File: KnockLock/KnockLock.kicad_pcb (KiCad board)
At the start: 2 copper layers, 90 x 60 mm, 60 parts, among them IC1 LM2575-3.3WT, IC2 ESP32-C3-WROOM-02-N4, J1 Boot Pins, J2 UART, J3 Battery Port, J4 Micro USB, J5 TBP04R12-500-03BE, M2 MountingHole_2.2mm_M2_ISO7380, Q1 BC547B, Q2 IRLML6402TRPBF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

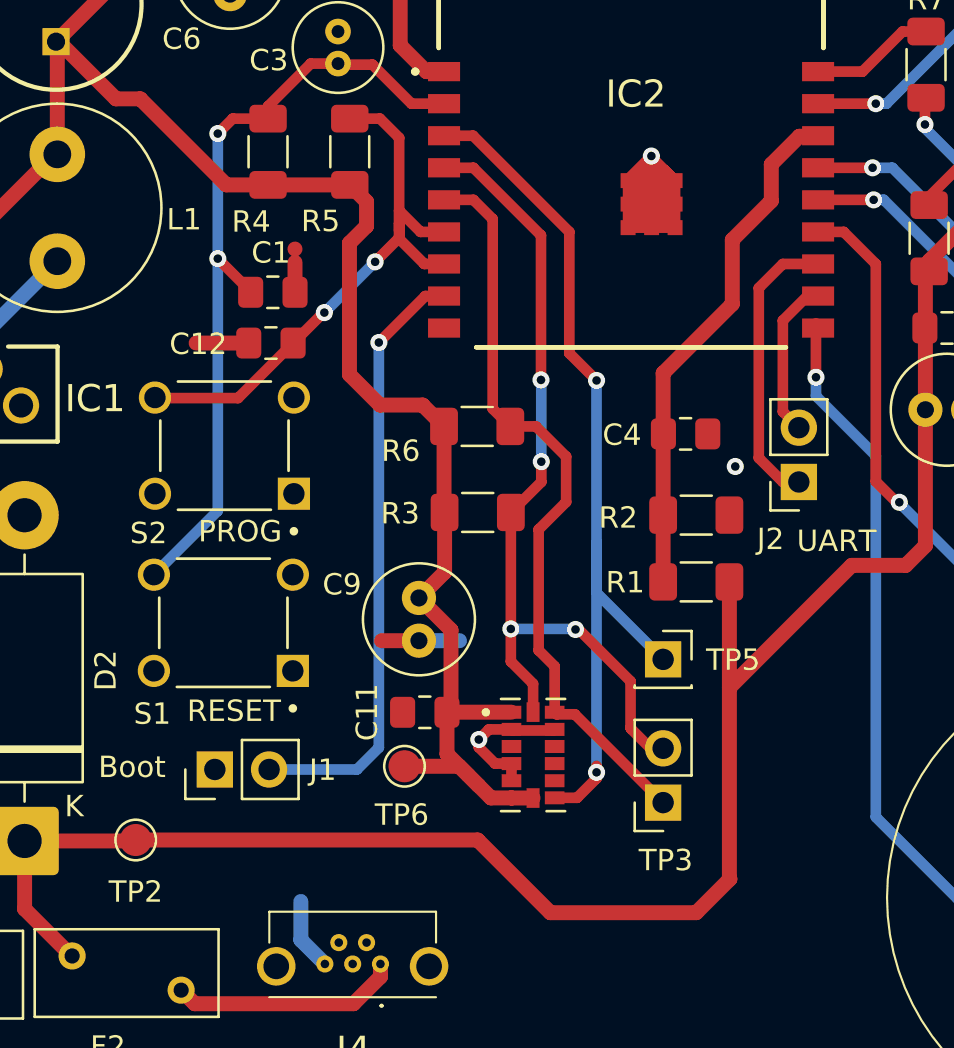
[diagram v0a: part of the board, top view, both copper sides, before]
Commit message: Thermal Adjustments
- added some additional vias to the heat sink of the MCU for better thermal relief into the button ground plane
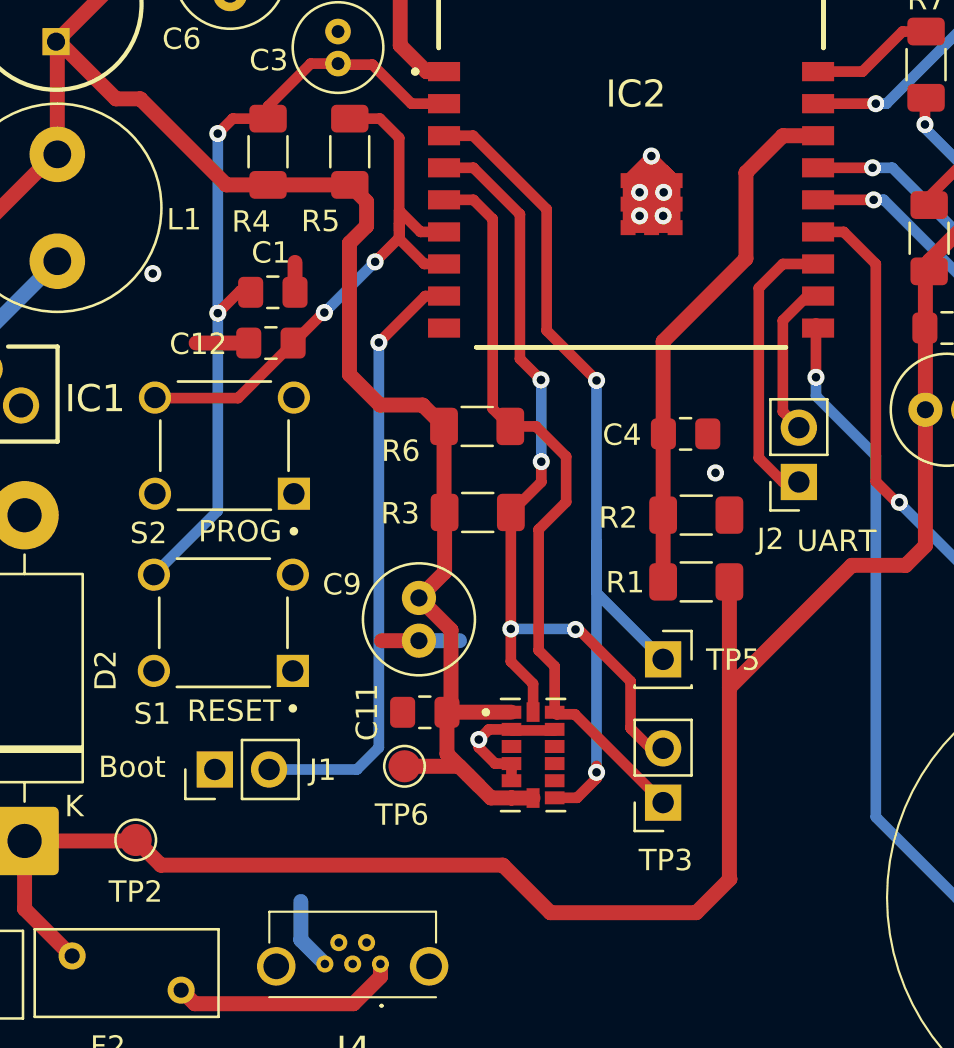
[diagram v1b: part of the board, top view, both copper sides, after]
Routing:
- net GND: vias 3 -> 8

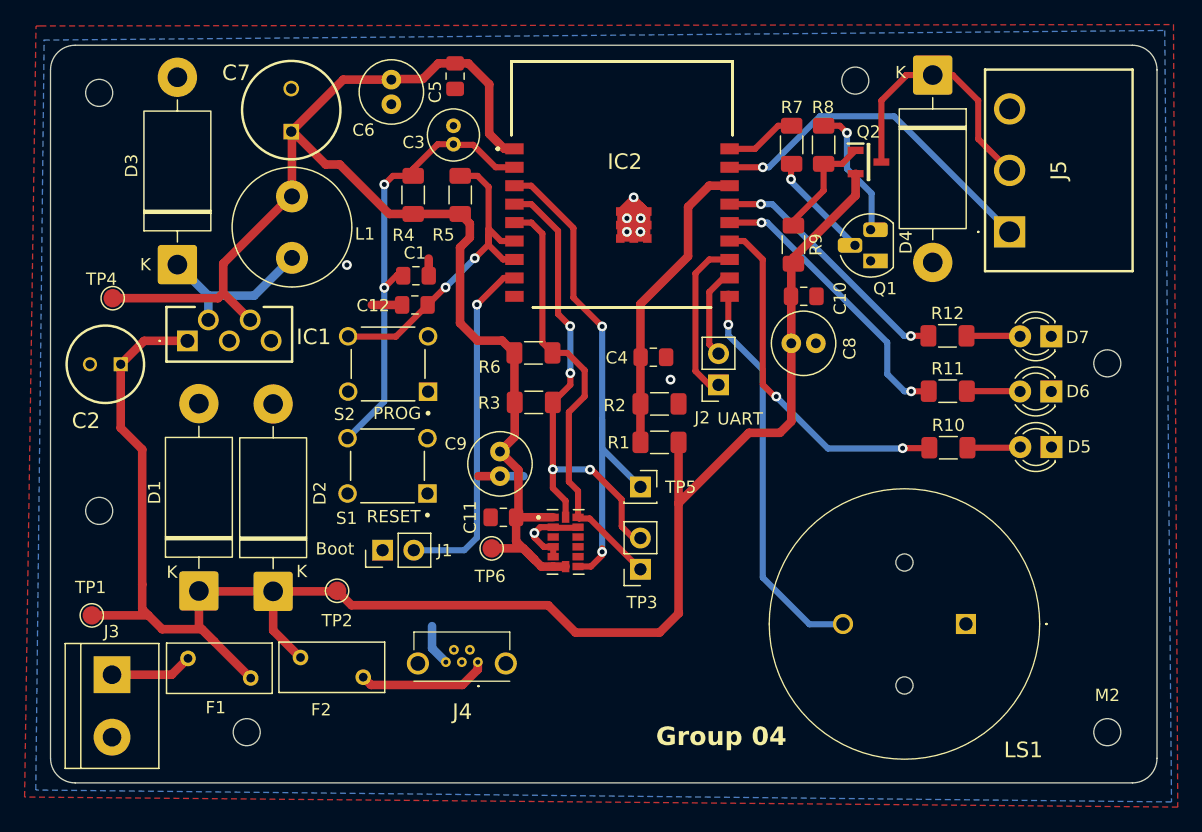
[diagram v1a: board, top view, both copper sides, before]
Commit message: Updates to 3D Model
- I made sure each component has a 3D model
- I changed the JST connector to the one the Lab has
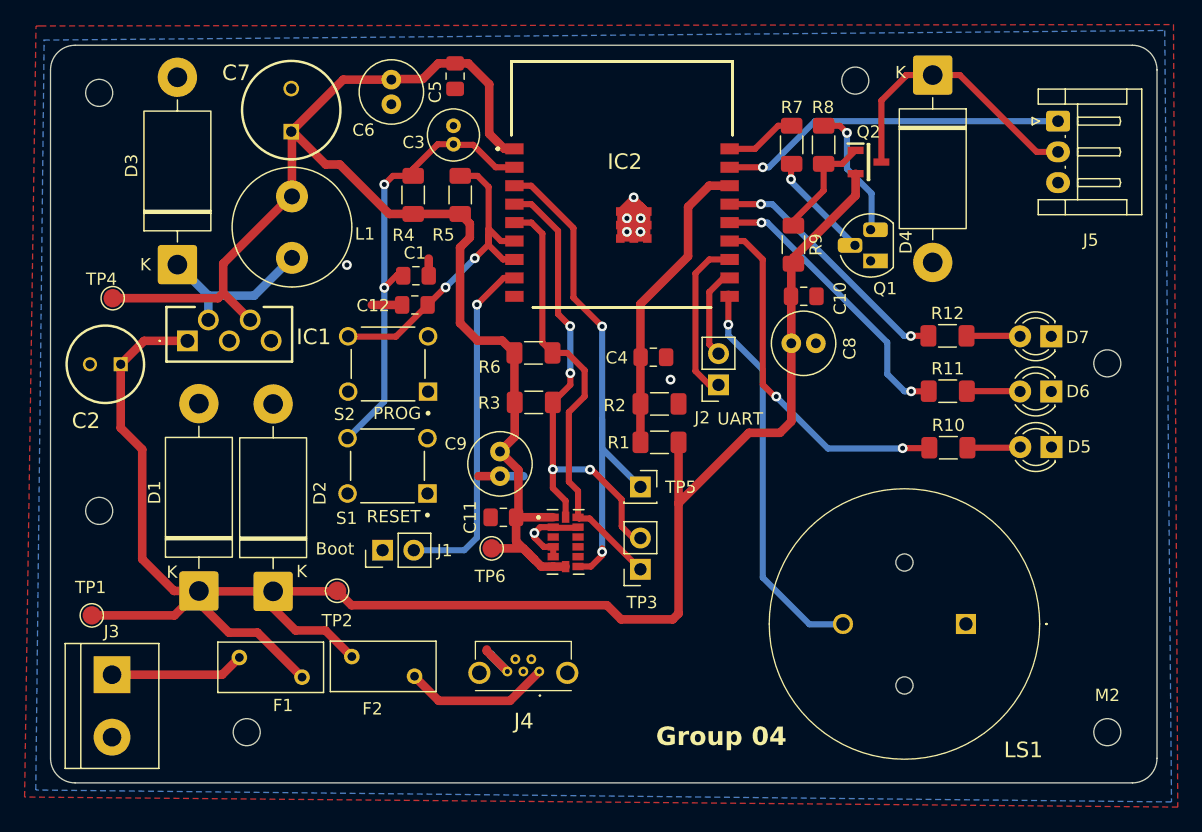
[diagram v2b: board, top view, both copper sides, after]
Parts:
- D1, D2: value 1N5822 -> 1N5908
- J5: footprint SamacSys_Parts:TBP04R1250003BE -> Connector_JST:JST_EH_S3B-EH_1x03_P2.50mm_Horizontal
- S2: value Prog But -> Programming Button
- moved J5 9.83 mm to (186.5, 75.3), turned to -90 degrees
- moved J4 5.06 mm to (143.0, 119.8)
- moved F1 4.18 mm to (119.9, 118.9)
- moved F2 4.18 mm to (134.2, 120.5)
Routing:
- net +5V: track 143.6 -> 148.4 mm
- net Net-(J3-Pin_1): track 6.73 -> 10.9 mm
- net Net-(F2-Pad1): track 10.7 -> 12.0 mm
- net GND: track 51.2 -> 52.2 mm
- net CONTROL: track 29.2 -> 28.3 mm
- net Net-(D4-K): track 22.0 -> 22.9 mm

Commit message: First Draft of Housing
- created a basic safe
- created a door with mounting holes, space for LED diffusion and built in button

- still need to do the hinge pins + slot for servo latch
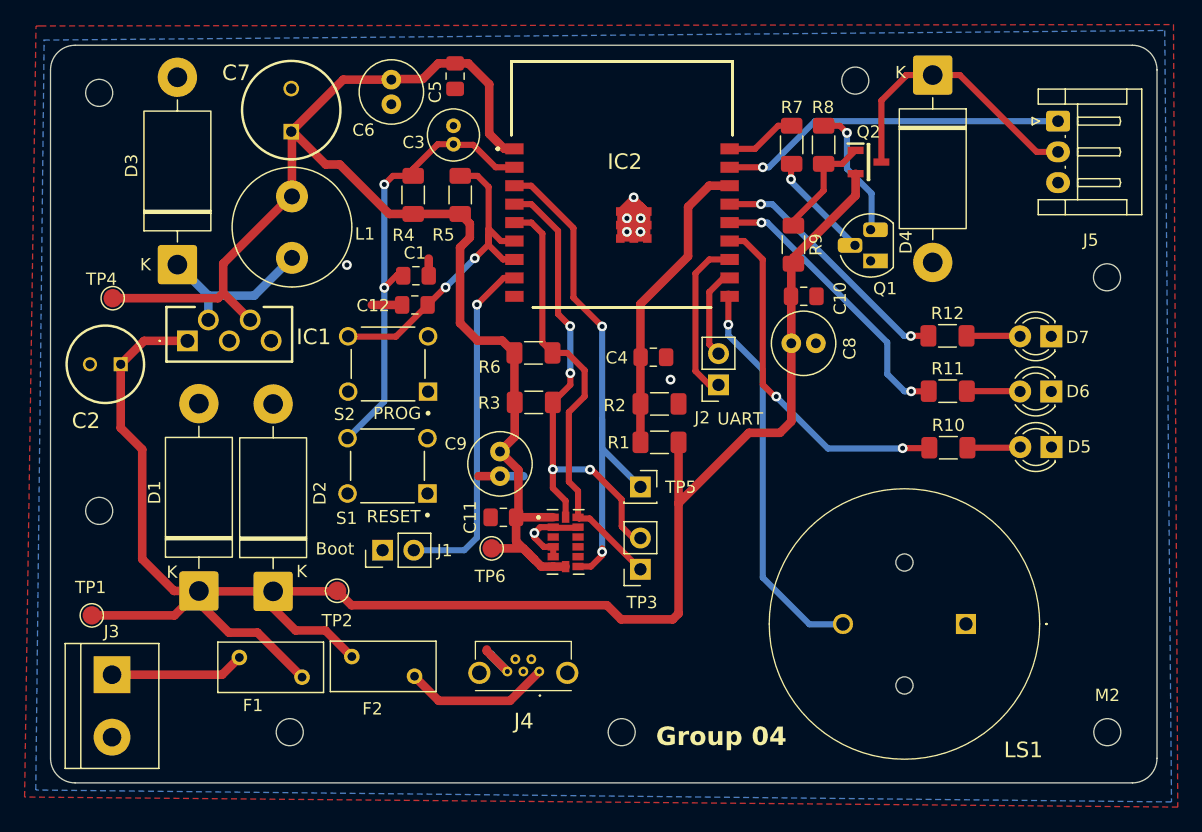
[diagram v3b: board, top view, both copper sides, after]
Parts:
- added REF**: MountingHole_2.2mm_M2_ISO7380, MountingHole:MountingHole_2.2mm_M2_ISO7380, F.Cu at (151.0, 125.0)
- moved M2 7.00 mm to (190.5, 88.0)
- moved REF** 3.50 mm to (124.0, 125.0)
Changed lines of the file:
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@@
 	(title_block
 		(title "KnockLock")
-		(date "2025-11-12")
+		(date "2025-11-16")
 		(rev "V2.0")
 		(company "HSRW")
@@
 		(tags "0ZRE BelFuse radial PTC")
 		(property "Reference" "F1"
-			(at 3.55 3.9 180)
+			(at 1.1 3.9 180)
 			(layer "F.SilkS")
 			(effects
@@
 	(footprint "MountingHole:MountingHole_2.2mm_M2_ISO7380"
 		(layer "F.Cu")
-		(at 120.5 125)
+		(at 124 125)
 		(descr "Mounting Hole 2.2mm, M2, no annular, generated by kicad-footprint-generator mountinghole.py")
 		(tags "mountinghole M2 ISO7380")
@@
 		)
 		(property "Value" "G-LED"
-			(at -3.659368 -1.597833 0)
+			(at -3.634368 5.402167 0)
 			(layer "F.Fab")
 			(effects
@@
 	(footprint "MountingHole:MountingHole_2.2mm_M2_ISO7380"
 		(layer "F.Cu")
-		(at 190.5 95)
+		(at 190.475 88)
 		(descr "Mounting Hole 2.2mm, M2, no annular, generated by kicad-footprint-generator mountinghole.py")
 		(tags "mountinghole M2 ISO7380")
@@
 		(embedded_fonts no)
 	)
+	(footprint "MountingHole:MountingHole_2.2mm_M2_ISO7380"
+		(layer "F.Cu")
+		(at 151 125)
+		(descr "Mounting Hole 2.2mm, M2, no annular, generated by kicad-footprint-generator mountinghole.py")
+		(tags "mountinghole M2 ISO7380")
+		(property "Reference" "REF**"
+			(at 4 0 0)
+			(layer "F.SilkS")
+			(hide yes)
+			(effects
+				(font
+					(size 1 1)
+					(thickness 0.15)
+				)
+			)
+		)
+		(property "Value" "MountingHole_2.2mm_M2_ISO7380"
+			(at 0 6 0)
+			(layer "F.Fab")
+			(effects
+				(font
+					(size 1 1)
+					(thickness 0.15)
+				)
+			)
+		)
+		(property "Datasheet" ""
+			(at 0 0 0)
+			(layer "F.Fab")
+			(hide yes)
+			(effects
+				(font
+					(size 1.27 1.27)
+					(thickness 0.15)
+				)
+			)
+		)
+		(property "Description" ""
+			(at 0 0 0)
+			(layer "F.Fab")
+			(hide yes)
+			(effects
+				(font
+					(size 1.27 1.27)
+					(thickness 0.15)
+				)
+			)
+		)
+		(attr exclude_from_pos_files exclude_from_bom)
+		(fp_circle
+			(center 0 0)
+			(end 1.75 0)
+			(stroke
+				(width 0.15)
+				(type solid)
+			)
+			(fill no)
+			(layer "Cmts.User")
+		)
+		(fp_circle
+			(center 0 0)
+			(end 2 0)
+			(stroke
+				(width 0.05)
+				(type solid)
+			)
+			(fill no)
+			(layer "F.CrtYd")
+		)
+		(fp_text user "${REFERENCE}"
+			(at 0 0 0)
+			(layer "F.Fab")
+			(effects
+				(font
+					(size 0.88 0.88)
+					(thickness 0.13)
+				)
+			)
+		)
+		(pad "" np_thru_hole circle
+			(at 0 0)
+			(size 2.2 2.2)
+			(drill 2.2)
+			(layers "*.Cu" "*.Mask")
+		)
+		(embedded_fonts no)
+	)
 	(footprint "Capacitor_THT:C_Radial_D5.0mm_H11.0mm_P2.00mm"
 		(layer "F.Cu")
@@
 	)
 	(gr_text "${PROJECTNAME} ${REVISION}\n"
-		(at 161.5 127 0)
+		(at 182.5 126.5 0)
 		(layer "B.SilkS")
 		(effects
@@
 	)
 	(gr_text "${ISSUE_DATE}"
-		(at 136 127 0)
+		(at 142 127.5 0)
 		(layer "B.SilkS")
 		(effects
